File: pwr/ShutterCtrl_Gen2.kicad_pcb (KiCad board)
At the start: 2 copper layers, 94 x 94 mm, 17 parts, among them K1 G2RL-2, Q1 BC817, Q2 TSM500P02CX, U1 S216S02

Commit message: First version of HW design
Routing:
- net GND: track 149.4 -> 155.3 mm
- net PE: track 50.7 -> 49.2 mm
- net L: track 46.3 -> 45.4 mm
- net L_RELAY: track 18.8 -> 18.3 mm
- net N: track 29.6 -> 29.1 mm
- net (no net): vias 0 -> 3
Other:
- board text added: "TpSz"

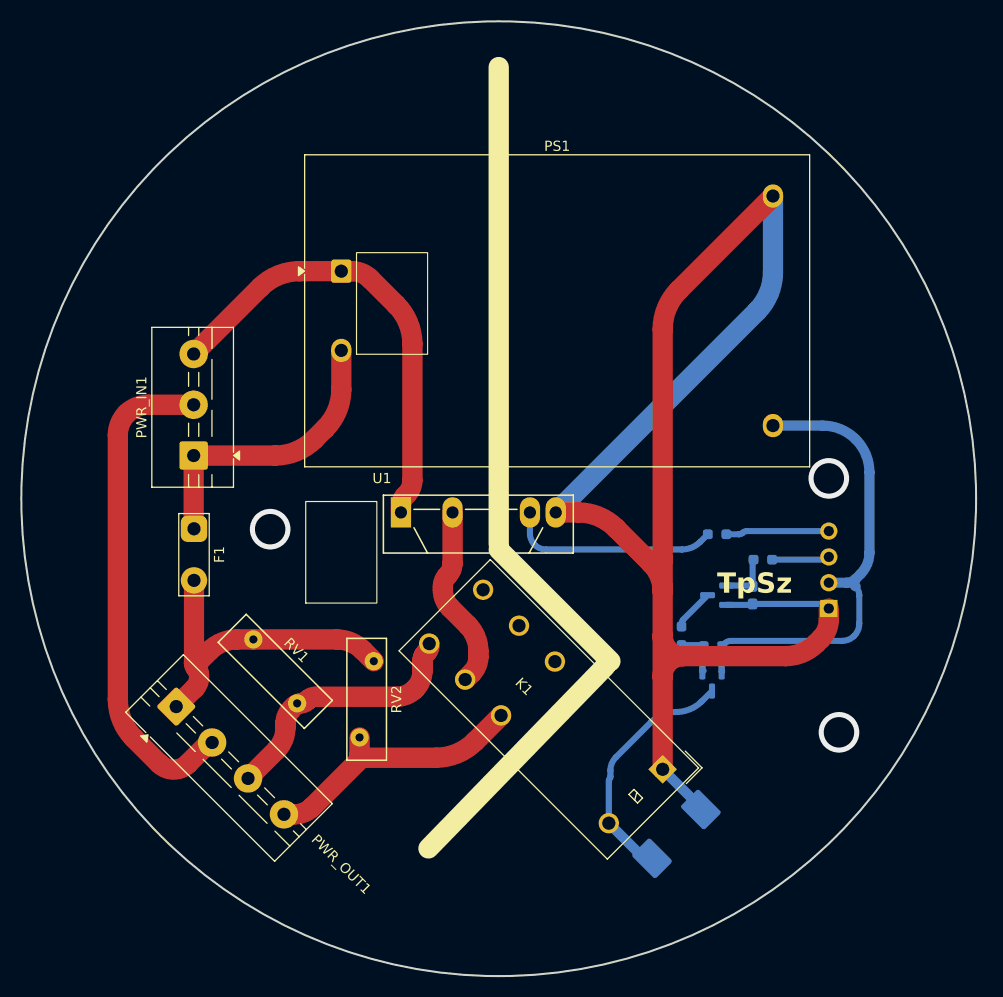
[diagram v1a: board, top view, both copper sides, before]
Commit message: PCB size was wrong, complete redesign...
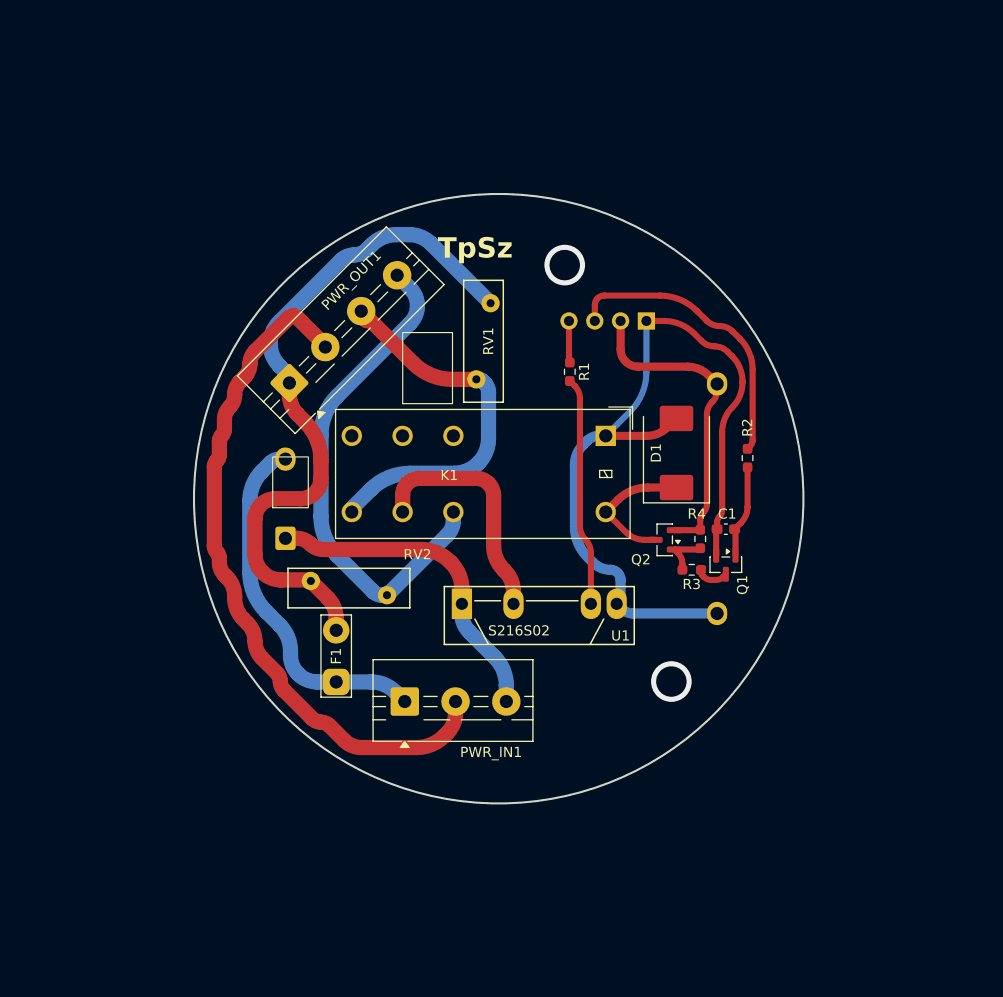
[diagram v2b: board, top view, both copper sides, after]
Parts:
- C1, D1, Q1, Q2, R1, R2, R3, R4: moved to F.Cu
- PS1: moved to B.Cu
- moved D1 37.5 mm to (114.0, 97.5), turned to 90 degrees
- moved RV1 36.5 mm to (94.3, 90.2), turned to 90 degrees
- moved PWR_OUT1 33.8 mm to (75.9, 90.6), turned to 45 degrees
- moved CTRL1 33.5 mm to (111.0, 84.5), turned to 90 degrees
- moved K1 33.3 mm to (107.0, 95.8), turned to -90 degrees
- moved PWR_IN1 31.9 mm to (87.2, 122.0), turned to 0 degrees
- moved PS1 26.9 mm to (75.5, 105.9)
- moved R1 21.6 mm to (103.5, 89.5), turned to -90 degrees
- moved F1 20.6 mm to (80.5, 120.0), turned to 90 degrees
- moved Q2 14.7 mm to (112.8, 106.0), turned to 180 degrees
- moved RV2 14.3 mm to (85.5, 111.5), turned to 180 degrees
- moved U1 10.8 mm to (92.9, 112.3)
- moved R4 10.6 mm to (116.3, 106.0), turned to -90 degrees
- moved R2 10.1 mm to (121.0, 98.0), turned to -90 degrees
- moved C1 7.01 mm to (118.9, 105.0), turned to 180 degrees
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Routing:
- net GND: track 155.3 -> 80.8 mm
- net N_OUT: track 33.3 -> 69.2 mm
- net RELAY_EN: track 5.68 -> 29.0 mm
- net UP: track 27.4 -> 49.5 mm
- net PE: track 49.2 -> 68.0 mm
- net +12V: track 48.5 -> 31.0 mm
- net L: track 45.4 -> 33.0 mm
- net DOWN: track 27.3 -> 38.3 mm
- net V_RELAY: track 24.1 -> 13.6 mm
- net N: track 29.1 -> 35.7 mm
- net SSR_EN: track 10.2 -> 4.11 mm
- net L_RELAY: track 18.3 -> 23.7 mm
- net Net-(Q1-B): track 5.19 -> 8.92 mm
- net Net-(R1-Pad2): track 21.0 -> 22.5 mm
- net Net-(Q1-C): track 4.12 -> 3.22 mm
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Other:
- board size 94 x 94 mm -> 60 x 60 mm
